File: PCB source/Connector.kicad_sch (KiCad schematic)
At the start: 1 part, among them J4 09031967921

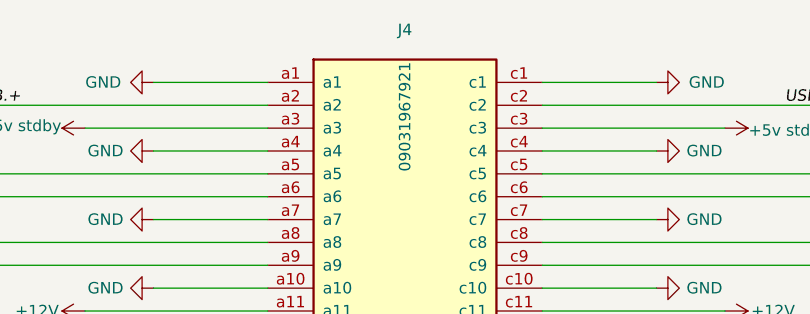
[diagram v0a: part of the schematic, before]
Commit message: change USB upstream pinout
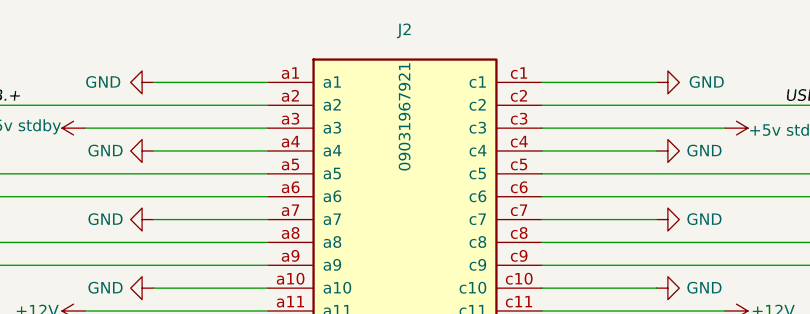
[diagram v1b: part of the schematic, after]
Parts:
- renumbered J4 to J2
